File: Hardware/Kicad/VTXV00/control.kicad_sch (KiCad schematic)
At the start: 37 parts, among them J1 FC, Q1 MMBT3904, SW1 BAND/CH, U1 AP2112K-3.3TRG1, U2 STM32F031G6U6

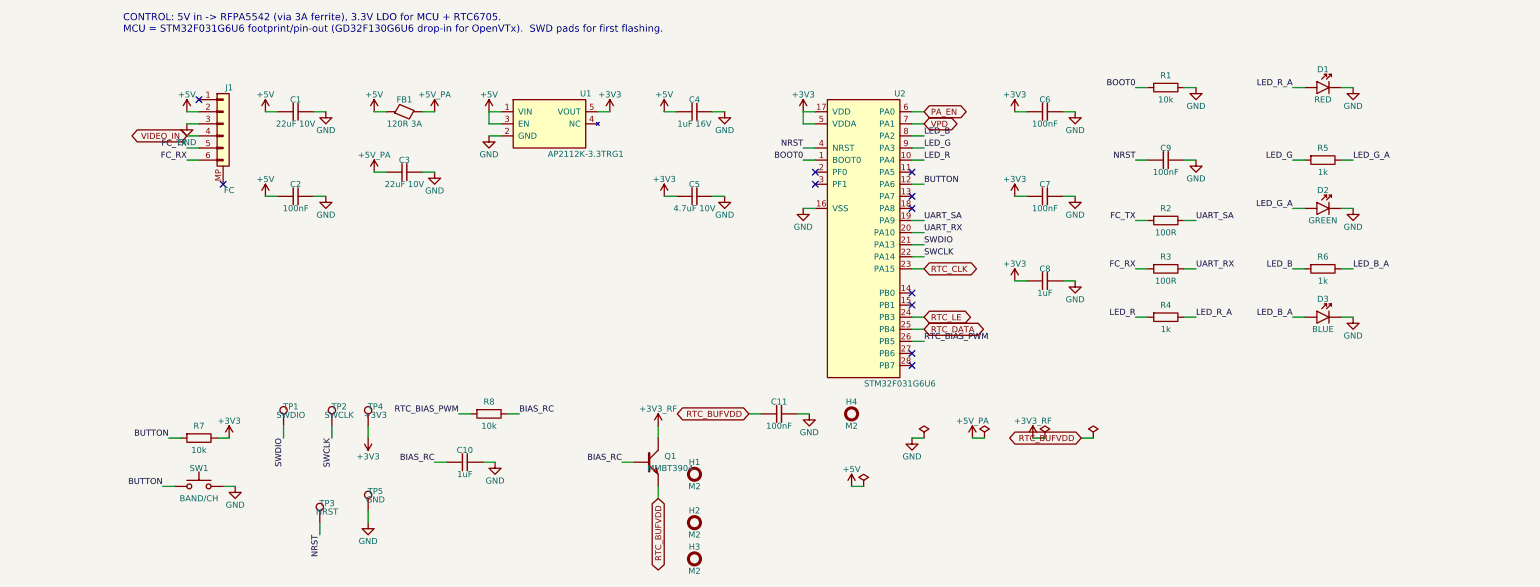
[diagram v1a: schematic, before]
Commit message: Boards follow the B0_EE part convention
- every real part uses the symbol/footprint/3D/datasheet named after its MPN in Kicad_Libs
- symbols keep only Reference, Value, Footprint, Datasheet, Description
  (MPN, Manufacturer, Verify, LCSC, Note fields removed; Verify notes moved to the Readme)
- schematic symbol caches rebuilt from the libraries, PCB footprints relinked with the
  same fields and 3D models as the library (connectivity unchanged)
- DNP and BOM attributes of the footprints match the symbols
- BOMs re-exported with kicad-cli
- ignore KiCad local history
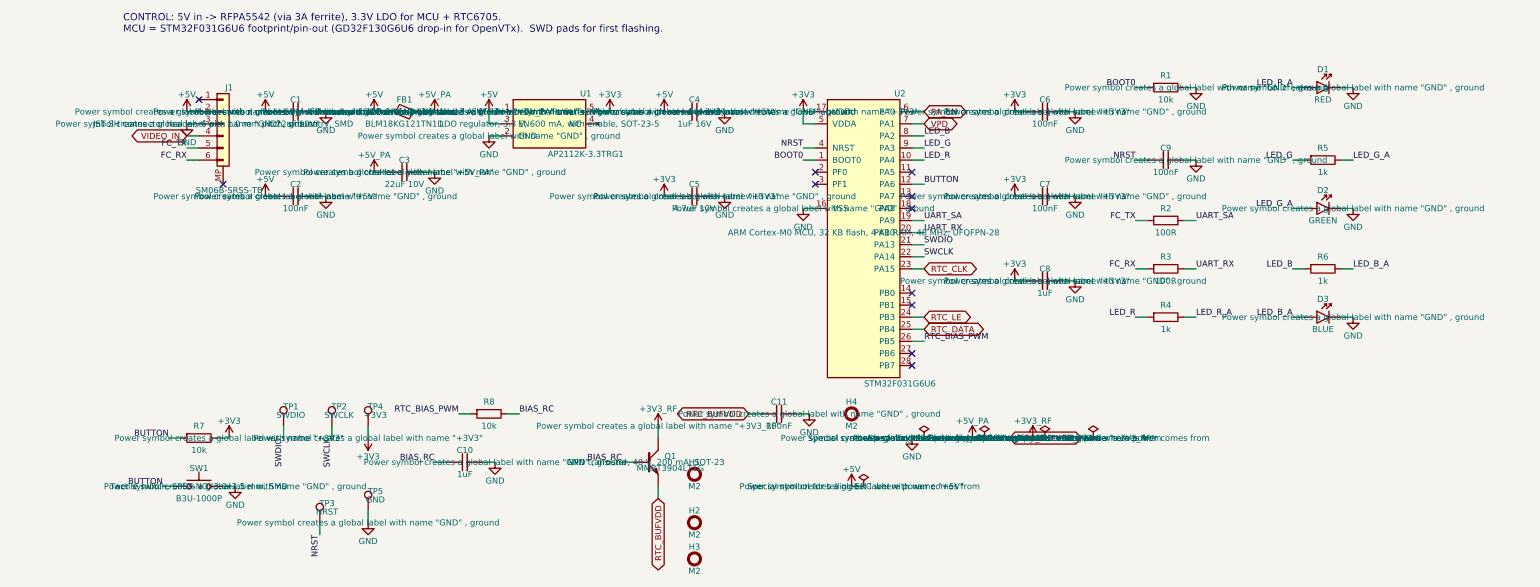
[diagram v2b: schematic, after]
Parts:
- FB1: value 120R 3A -> BLM18KG121TN1D; footprint eChoke:L_0603_1608Metric -> eFerrite:BLM18KG121TN1D; symbol eChoke:FB -> eFerrite:BLM18KG121TN1D; MPN BLM18KG121TN1D -> (none); Manufacturer Murata -> (none)
- H1, H2, H3, H4, TP1, TP2, TP3, TP4, TP5: now left out of the parts list
- J1: value FC -> SM06B-SRSS-TB; footprint eConnector:JST_SH_SM06B-SRSS-TB_1x06-1MP_P1.00mm_Horizontal -> eConnector:SM06B-SRSS-TB; symbol eConnector:JST_SH_SM06B-SRSS-TB -> eConnector:SM06B-SRSS-TB; MPN SM06B-SRSS-TB(LF)(SN) -> (none); Manufacturer JST -> (none)
- Q1: value MMBT3904 -> MMBT3904LT1G; footprint eTransistor:SOT-23 -> eTransistor:MMBT3904LT1G; symbol eTransistor:MMBT3904 -> eTransistor:MMBT3904LT1G; LCSC C20526 -> (none); MPN MMBT3904LT1G -> (none); Manufacturer onsemi -> (none)
- SW1: value BAND/CH -> B3U-1000P; footprint eSwitch:SW_SPST_B3U-1000P -> eSwitch:B3U-1000P; symbol eSwitch:SW_Push -> eSwitch:B3U-1000P; MPN B3U-1000P -> (none); Manufacturer Omron -> (none)
- U1: footprint eLinearReg:SOT-23-5 -> eLinearReg:AP2112K-3.3TRG1; LCSC C51118 -> (none); MPN AP2112K-3.3TRG1 -> (none); Manufacturer Diodes Inc -> (none)
- U2: footprint eMCU:QFN-28_4x4mm_P0.5mm -> eMCU:STM32F031G6U6; MPN STM32F031G6U6 -> (none); Manufacturer STMicroelectronics -> (none)

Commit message: Cleared all the descriptions and started Power section for FCV
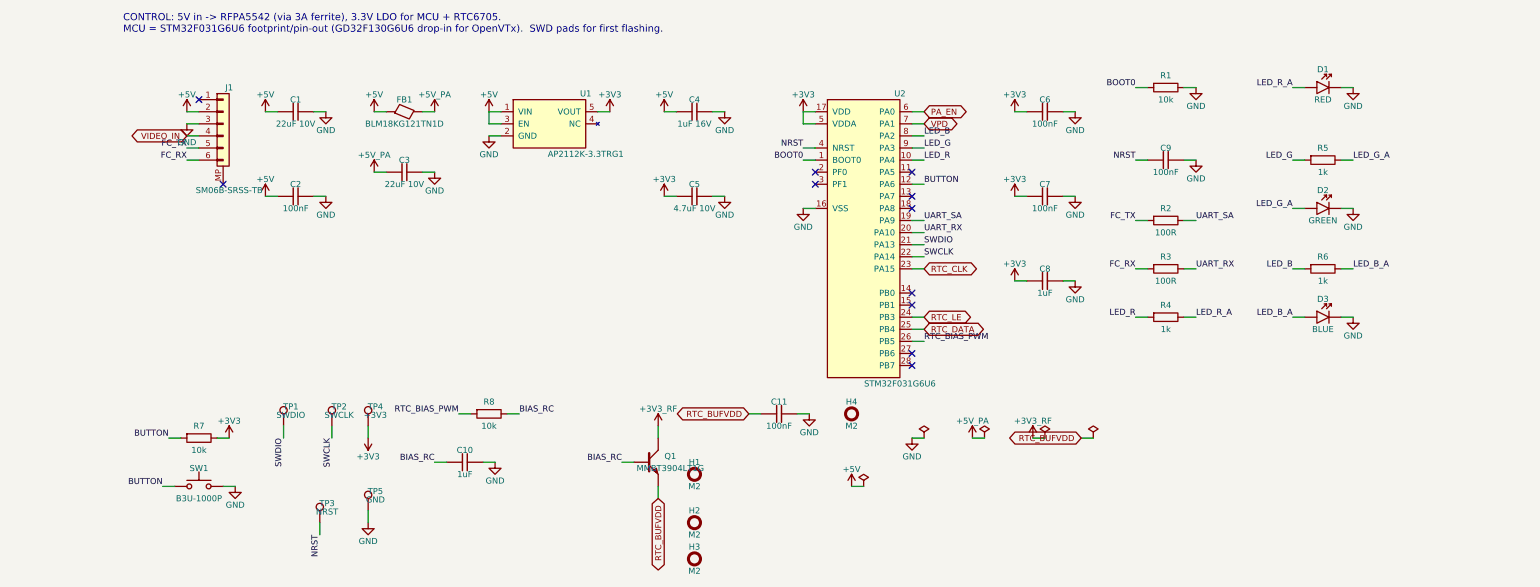
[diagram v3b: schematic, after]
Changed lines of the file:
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@@
 			(show_name no)
 			(do_not_autoplace no)
+			(hide yes)
 			(effects
 				(font
@@
 			(show_name no)
 			(do_not_autoplace no)
+			(hide yes)
 			(effects
 				(font
@@
 			(show_name no)
 			(do_not_autoplace no)
+			(hide yes)
 			(effects
 				(font
@@
 			(show_name no)
 			(do_not_autoplace no)
+			(hide yes)
 			(effects
 				(font
@@
 			(show_name no)
 			(do_not_autoplace no)
+			(hide yes)
 			(effects
 				(font
@@
 			(show_name no)
 			(do_not_autoplace no)
+			(hide yes)
 			(effects
 				(font
@@
 			(show_name no)
 			(do_not_autoplace no)
+			(hide yes)
 			(effects
 				(font
@@
 			(show_name no)
 			(do_not_autoplace no)
+			(hide yes)
 			(effects
 				(font
@@
 			(show_name no)
 			(do_not_autoplace no)
+			(hide yes)
 			(effects
 				(font
@@
 			(show_name no)
 			(do_not_autoplace no)
+			(hide yes)
 			(effects
 				(font
@@
 			(show_name no)
 			(do_not_autoplace no)
+			(hide yes)
 			(effects
 				(font
@@
 			(show_name no)
 			(do_not_autoplace no)
+			(hide yes)
 			(effects
 				(font
@@
 			(show_name no)
 			(do_not_autoplace no)
+			(hide yes)
 			(effects
 				(font
@@
 			(show_name no)
 			(do_not_autoplace no)
+			(hide yes)
 			(effects
 				(font
@@
 			(show_name no)
 			(do_not_autoplace no)
+			(hide yes)
 			(effects
 				(font
@@
 			(show_name no)
 			(do_not_autoplace no)
+			(hide yes)
 			(effects
 				(font
@@
 			(show_name no)
 			(do_not_autoplace no)
+			(hide yes)
 			(effects
 				(font
@@
 			(show_name no)
 			(do_not_autoplace no)
+			(hide yes)
 			(effects
 				(font
@@
 			(show_name no)
 			(do_not_autoplace no)
+			(hide yes)
 			(effects
 				(font
@@
 			(show_name no)
 			(do_not_autoplace no)
+			(hide yes)
 			(effects
 				(font
@@
 			(show_name no)
 			(do_not_autoplace no)
+			(hide yes)
 			(effects
 				(font
@@
 			(show_name no)
 			(do_not_autoplace no)
+			(hide yes)
 			(effects
 				(font
@@
 			(show_name no)
 			(do_not_autoplace no)
+			(hide yes)
 			(effects
 				(font
@@
 			(show_name no)
 			(do_not_autoplace no)
+			(hide yes)
 			(effects
 				(font
@@
 			(show_name no)
 			(do_not_autoplace no)
+			(hide yes)
 			(effects
 				(font
@@
 			(show_name no)
 			(do_not_autoplace no)
+			(hide yes)
 			(effects
 				(font
@@
 			(show_name no)
 			(do_not_autoplace no)
+			(hide yes)
 			(effects
 				(font
@@
 			(show_name no)
 			(do_not_autoplace no)
+			(hide yes)
 			(effects
 				(font
@@
 			(show_name no)
 			(do_not_autoplace no)
+			(hide yes)
 			(effects
 				(font
@@
 			(show_name no)
 			(do_not_autoplace no)
+			(hide yes)
 			(effects
 				(font
@@
 			(show_name no)
 			(do_not_autoplace no)
+			(hide yes)
 			(effects
 				(font
@@
 			(show_name no)
 			(do_not_autoplace no)
+			(hide yes)
 			(effects
 				(font
@@
 			(show_name no)
 			(do_not_autoplace no)
+			(hide yes)
 			(effects
 				(font
@@
 			(show_name no)
 			(do_not_autoplace no)
+			(hide yes)
 			(effects
 				(font
@@
 			(show_name no)
 			(do_not_autoplace no)
+			(hide yes)
 			(effects
 				(font
@@
 			(show_name no)
 			(do_not_autoplace no)
+			(hide yes)
 			(effects
 				(font
@@
 			(show_name no)
 			(do_not_autoplace no)
+			(hide yes)
 			(effects
 				(font
@@
 			(show_name no)
 			(do_not_autoplace no)
+			(hide yes)
 			(effects
 				(font
@@
 			(show_name no)
 			(do_not_autoplace no)
+			(hide yes)
 			(effects
 				(font
@@
 			(show_name no)
 			(do_not_autoplace no)
+			(hide yes)
 			(effects
 				(font
@@
 			(show_name no)
 			(do_not_autoplace no)
+			(hide yes)
 			(effects
 				(font
@@
 			(show_name no)
 			(do_not_autoplace no)
+			(hide yes)
 			(effects
 				(font
@@
 			(show_name no)
 			(do_not_autoplace no)
+			(hide yes)
 			(effects
 				(font
@@
 			(show_name no)
 			(do_not_autoplace no)
+			(hide yes)
 			(effects
 				(font
@@
 			(show_name no)
 			(do_not_autoplace no)
+			(hide yes)
 			(effects
 				(font
@@
 			(show_name no)
 			(do_not_autoplace no)
+			(hide yes)
 			(effects
 				(font
@@
 			(show_name no)
 			(do_not_autoplace no)
+			(hide yes)
 			(effects
 				(font
@@
 			(show_name no)
 			(do_not_autoplace no)
+			(hide yes)
 			(effects
 				(font
@@
 			(show_name no)
 			(do_not_autoplace no)
+			(hide yes)
 			(effects
 				(font
@@
 			(show_name no)
 			(do_not_autoplace no)
+			(hide yes)
 			(effects
 				(font
@@
 			(show_name no)
 			(do_not_autoplace no)
+			(hide yes)
 			(effects
 				(font
@@
 			(show_name no)
 			(do_not_autoplace no)
+			(hide yes)
 			(effects
 				(font
